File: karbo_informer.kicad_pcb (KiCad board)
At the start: 2 copper layers, 12 parts, among them IC1 MAX7219, IC2 MAX7219, P1 USB_OTG

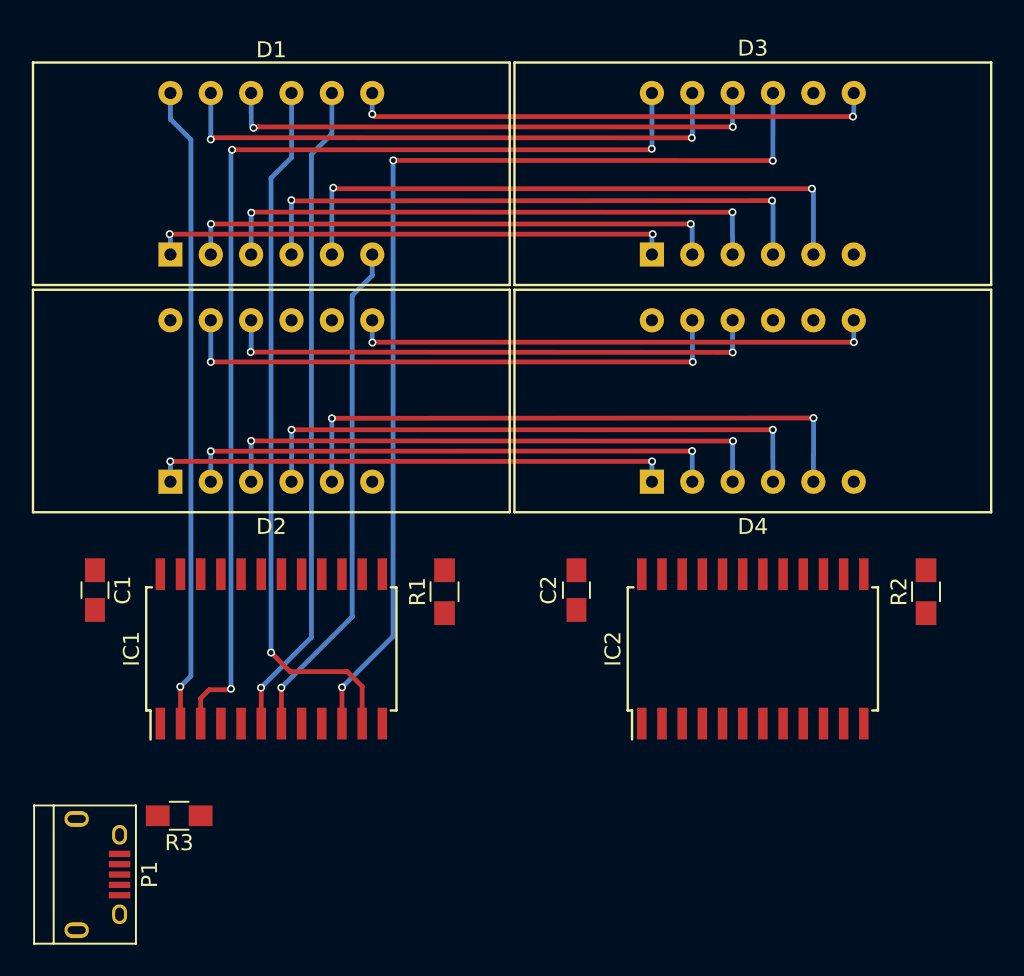
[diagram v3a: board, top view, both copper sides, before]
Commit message: Wire for DIG7 to MAX7219 in the buy line
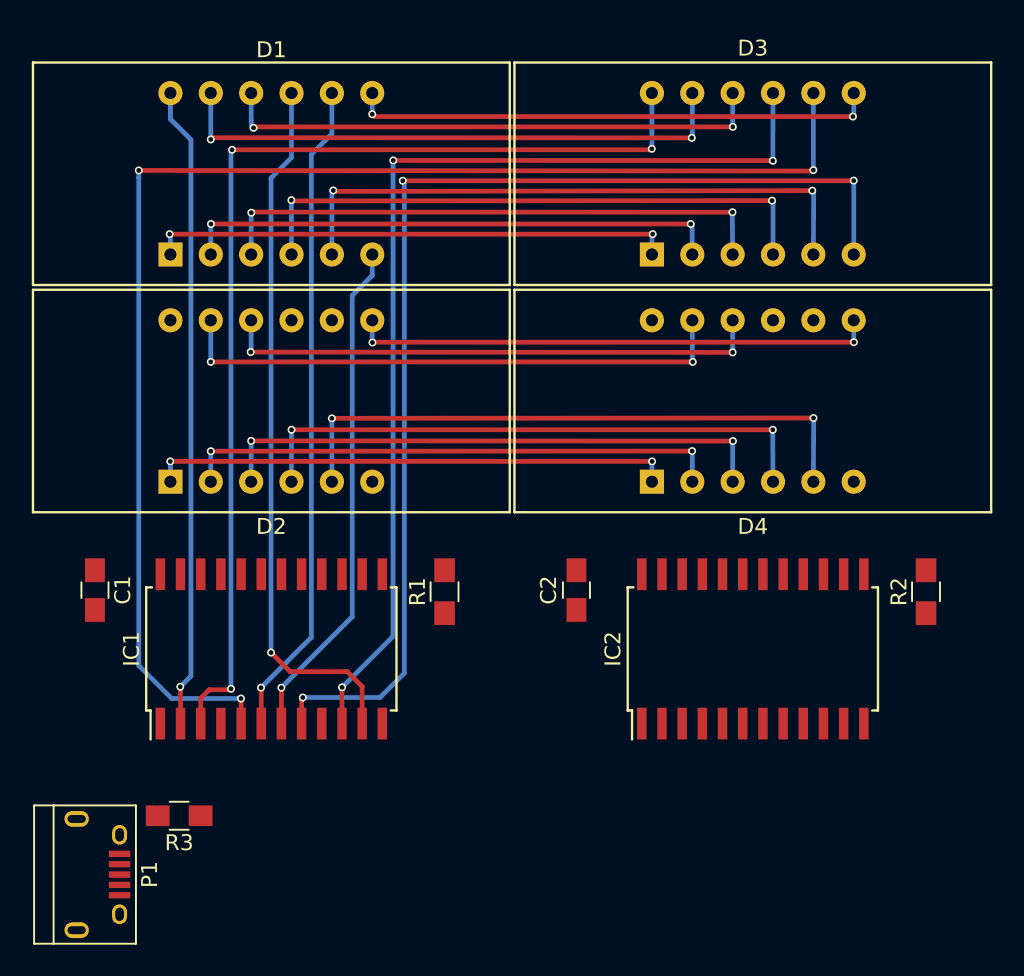
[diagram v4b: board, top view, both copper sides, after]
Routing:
- net /B_DIG_6: track 0.00 -> 87.4 mm, vias 0 -> 3
- net /B_DIG_7: track 0.00 -> 72.8 mm, vias 0 -> 3
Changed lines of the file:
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@@
   (general
     (links 69)
-    (no_connects 47)
+    (no_connects 45)
     (area 0 0 0 0)
     (thickness 1.6)
     (drawings 0)
-    (tracks 157)
+    (tracks 181)
     (zones 0)
     (modules 12)
@@
   (segment (start 42.07 33.98) (end 42.06 30.56) (width 0.3) (layer B.Cu) (net 4))
   (segment (start 42.06 30.56) (end 42.07 30.55) (width 0.3) (layer B.Cu) (net 4))
-  (segment (start 44.61 33.98) (end 44.61 29.87) (width 0.3) (layer B.Cu) (net 5))
-  (segment (start 74.91 29.93) (end 74.91 33.98) (width 0.3) (layer B.Cu) (net 5))
-  (segment (start 74.82 29.84) (end 74.91 29.93) (width 0.3) (layer B.Cu) (net 5))
-  (via (at 74.82 29.84) (size 0.5) (drill 0.3) (layers F.Cu B.Cu) (net 5))
-  (segment (start 44.76 29.84) (end 74.82 29.84) (width 0.3) (layer F.Cu) (net 5))
-  (segment (start 44.7 29.78) (end 44.76 29.84) (width 0.3) (layer F.Cu) (net 5))
-  (via (at 44.7 29.78) (size 0.5) (drill 0.3) (layers F.Cu B.Cu) (net 5))
-  (segment (start 44.61 29.87) (end 44.7 29.78) (width 0.3) (layer B.Cu) (net 5))
+  (segment (start 44.61 33.98) (end 44.61 30.04) (width 0.3) (layer B.Cu) (net 5) (status 400000))
+  (segment (start 74.93 30.05) (end 74.91 33.98) (width 0.3) (layer B.Cu) (net 5) (status 800000))
+  (segment (start 74.84 29.96) (end 74.93 30.05) (width 0.3) (layer B.Cu) (net 5))
+  (via (at 74.84 29.96) (size 0.5) (drill 0.3) (layers F.Cu B.Cu) (net 5))
+  (segment (start 44.76 30.01) (end 74.84 29.96) (width 0.3) (layer F.Cu) (net 5))
+  (segment (start 44.7 29.95) (end 44.76 30.01) (width 0.3) (layer F.Cu) (net 5))
+  (via (at 44.7 29.95) (size 0.5) (drill 0.3) (layers F.Cu B.Cu) (net 5))
+  (segment (start 44.61 30.04) (end 44.7 29.95) (width 0.3) (layer B.Cu) (net 5))
   (segment (start 47.15 33.98) (end 47.15 35.3) (width 0.3) (layer B.Cu) (net 6))
   (segment (start 41.435 61.245) (end 41.435 63.5) (width 0.3) (layer F.Cu) (net 6))
@@
   (segment (start 47.18 39.5) (end 77.46 39.5) (width 0.3) (layer F.Cu) (net 24))
   (via (at 47.16 39.52) (size 0.5) (drill 0.3) (layers F.Cu B.Cu) (net 24))
+  (segment (start 74.91 23.82) (end 74.91 28.67) (width 0.3) (layer B.Cu) (net 25) (status 400000))
+  (segment (start 38.895 61.925) (end 38.895 63.5) (width 0.3) (layer F.Cu) (net 25) (status 800000))
+  (segment (start 38.89 61.92) (end 38.895 61.925) (width 0.3) (layer F.Cu) (net 25))
+  (via (at 38.89 61.92) (size 0.5) (drill 0.3) (layers F.Cu B.Cu) (net 25))
+  (segment (start 34.53 61.92) (end 38.89 61.92) (width 0.3) (layer B.Cu) (net 25))
+  (segment (start 32.46 59.85) (end 34.53 61.92) (width 0.3) (layer B.Cu) (net 25))
+  (segment (start 32.46 29.15) (end 32.46 59.85) (width 0.3) (layer B.Cu) (net 25))
+  (segment (start 32.46 28.69) (end 32.46 29.15) (width 0.3) (layer B.Cu) (net 25))
+  (via (at 32.46 28.69) (size 0.5) (drill 0.3) (layers F.Cu B.Cu) (net 25))
+  (segment (start 74.85 28.73) (end 32.46 28.69) (width 0.3) (layer F.Cu) (net 25))
+  (segment (start 74.91 28.67) (end 74.85 28.73) (width 0.3) (layer F.Cu) (net 25))
+  (via (at 74.91 28.67) (size 0.5) (drill 0.3) (layers F.Cu B.Cu) (net 25))
   (segment (start 36.355 61.905) (end 36.355 63.5) (width 0.3) (layer F.Cu) (net 26))
   (segment (start 36.89 61.37) (end 36.355 61.905) (width 0.3) (layer F.Cu) (net 26))
@@
   (segment (start 48.47 28.06) (end 48.46 28.07) (width 0.3) (layer B.Cu) (net 27))
   (segment (start 72.37 23.82) (end 72.36 28.08) (width 0.3) (layer B.Cu) (net 27) (status 400000))
+  (segment (start 77.45 33.98) (end 77.45 29.33) (width 0.3) (layer B.Cu) (net 33) (status 400000))
+  (segment (start 42.705 61.935) (end 42.705 63.5) (width 0.3) (layer F.Cu) (net 33) (status 800000))
+  (segment (start 42.78 61.86) (end 42.705 61.935) (width 0.3) (layer F.Cu) (net 33))
+  (via (at 42.78 61.86) (size 0.5) (drill 0.3) (layers F.Cu B.Cu) (net 33))
+  (segment (start 47.64 61.86) (end 42.78 61.86) (width 0.3) (layer B.Cu) (net 33))
+  (segment (start 49.17 60.33) (end 47.64 61.86) (width 0.3) (layer B.Cu) (net 33))
+  (segment (start 49.17 29.44) (end 49.17 60.33) (width 0.3) (layer B.Cu) (net 33))
+  (segment (start 49.07 29.34) (end 49.17 29.44) (width 0.3) (layer B.Cu) (net 33))
+  (via (at 49.07 29.34) (size 0.5) (drill 0.3) (layers F.Cu B.Cu) (net 33))
+  (segment (start 77.44 29.34) (end 49.07 29.34) (width 0.3) (layer F.Cu) (net 33))
+  (segment (start 77.45 29.33) (end 77.44 29.34) (width 0.3) (layer F.Cu) (net 33))
+  (via (at 77.45 29.33) (size 0.5) (drill 0.3) (layers F.Cu B.Cu) (net 33))
 )

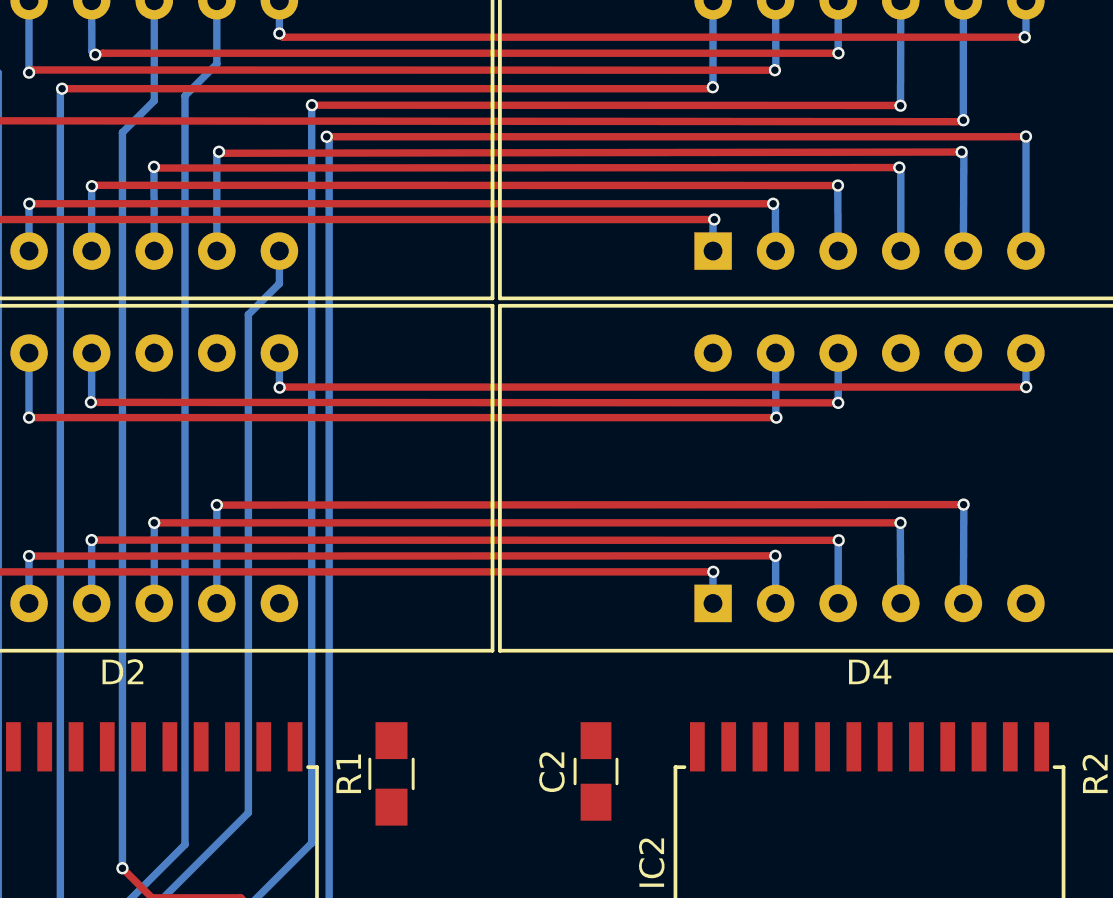
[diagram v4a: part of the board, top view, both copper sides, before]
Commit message: Wire for SEG_G to MAX7219 in the buy line
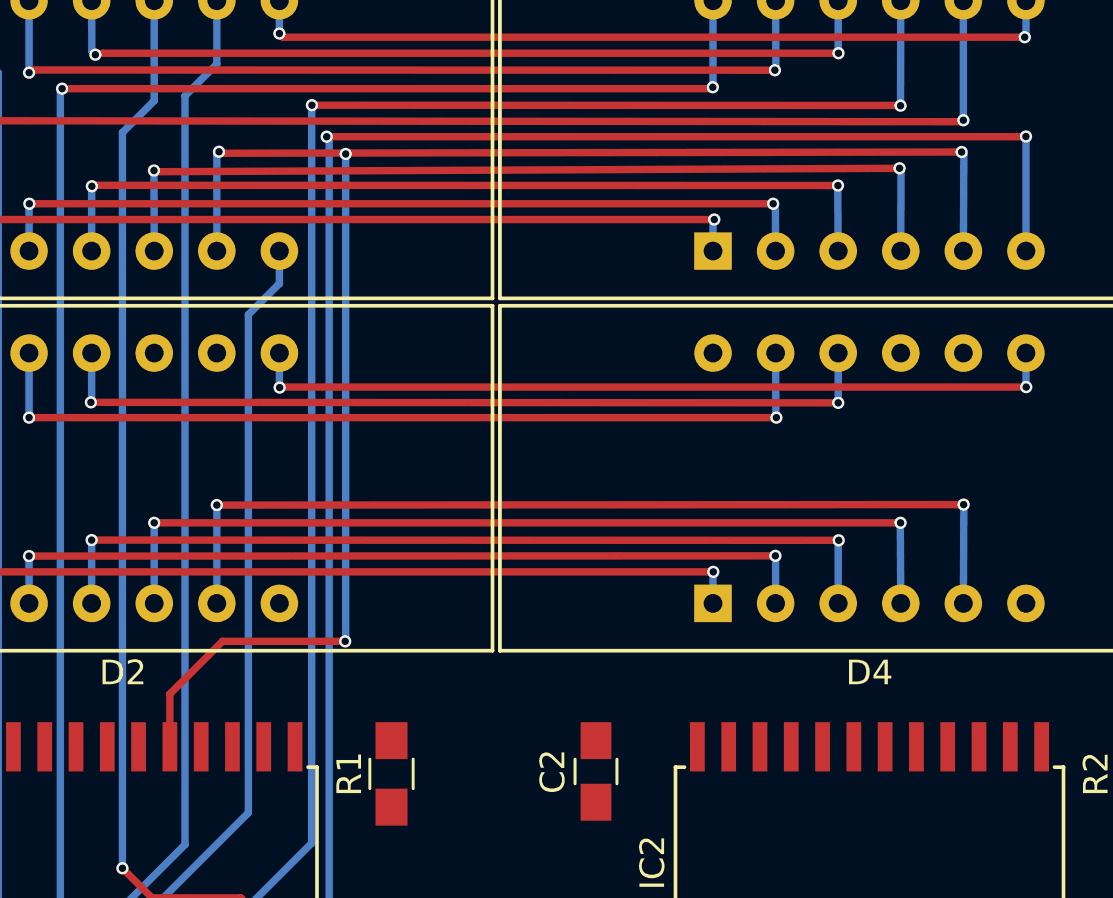
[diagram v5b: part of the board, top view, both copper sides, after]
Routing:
- net /B_SEG_G: track 38.3 -> 68.3 mm, vias 2 -> 4
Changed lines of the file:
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@@
   (general
     (links 69)
-    (no_connects 45)
+    (no_connects 44)
     (area 0 0 0 0)
     (thickness 1.6)
     (drawings 0)
-    (tracks 181)
+    (tracks 191)
     (zones 0)
     (modules 12)
@@
   (segment (start 37 32.06) (end 67.19 32.06) (width 0.3) (layer F.Cu) (net 3))
   (via (at 37 32.06) (size 0.5) (drill 0.3) (layers F.Cu B.Cu) (net 3))
-  (via (at 42.06 30.56) (size 0.5) (drill 0.3) (layers F.Cu B.Cu) (net 4))
-  (segment (start 72.37 33.98) (end 72.37 30.65) (width 0.3) (layer B.Cu) (net 4))
-  (segment (start 72.31 30.59) (end 72.37 30.65) (width 0.3) (layer B.Cu) (net 4))
-  (via (at 72.31 30.59) (size 0.5) (drill 0.3) (layers F.Cu B.Cu) (net 4))
-  (segment (start 42.11 30.61) (end 72.31 30.59) (width 0.3) (layer F.Cu) (net 4))
-  (segment (start 42.11 30.61) (end 42.06 30.56) (width 0.3) (layer F.Cu) (net 4))
-  (segment (start 42.07 33.98) (end 42.06 30.56) (width 0.3) (layer B.Cu) (net 4))
-  (segment (start 42.06 30.56) (end 42.07 30.55) (width 0.3) (layer B.Cu) (net 4))
+  (via (at 42.06 30.71) (size 0.5) (drill 0.3) (layers F.Cu B.Cu) (net 4))
+  (segment (start 72.37 33.98) (end 72.38 30.68) (width 0.3) (layer B.Cu) (net 4) (status 400000))
+  (segment (start 72.32 30.62) (end 72.38 30.68) (width 0.3) (layer B.Cu) (net 4))
+  (via (at 72.32 30.62) (size 0.5) (drill 0.3) (layers F.Cu B.Cu) (net 4))
+  (segment (start 42.11 30.76) (end 72.32 30.62) (width 0.3) (layer F.Cu) (net 4))
+  (segment (start 42.11 30.76) (end 42.06 30.71) (width 0.3) (layer F.Cu) (net 4))
+  (segment (start 42.07 33.98) (end 42.06 30.71) (width 0.3) (layer B.Cu) (net 4) (status 400000))
+  (segment (start 42.06 30.71) (end 42.07 30.7) (width 0.3) (layer B.Cu) (net 4))
+  (via (at 49.84 30.04) (size 0.5) (drill 0.3) (layers F.Cu B.Cu) (net 5))
+  (segment (start 42.705 51.955) (end 44.84 49.82) (width 0.3) (layer F.Cu) (net 5))
+  (segment (start 44.84 49.82) (end 49.82 49.82) (width 0.3) (layer F.Cu) (net 5))
+  (via (at 49.82 49.82) (size 0.5) (drill 0.3) (layers F.Cu B.Cu) (net 5))
+  (segment (start 49.82 49.82) (end 49.84 49.8) (width 0.3) (layer B.Cu) (net 5))
+  (segment (start 49.84 49.8) (end 49.84 30.04) (width 0.3) (layer B.Cu) (net 5))
+  (segment (start 42.705 54.1) (end 42.705 51.955) (width 0.3) (layer F.Cu) (net 5) (status 400000))
+  (segment (start 49.829936 30.029936) (end 49.829936 30.001573) (width 0.3) (layer F.Cu) (net 5))
+  (segment (start 49.84 30.04) (end 49.829936 30.029936) (width 0.3) (layer F.Cu) (net 5))
   (segment (start 44.61 33.98) (end 44.61 30.04) (width 0.3) (layer B.Cu) (net 5) (status 400000))
   (segment (start 74.93 30.05) (end 74.91 33.98) (width 0.3) (layer B.Cu) (net 5) (status 800000))
   (segment (start 74.84 29.96) (end 74.93 30.05) (width 0.3) (layer B.Cu) (net 5))
   (via (at 74.84 29.96) (size 0.5) (drill 0.3) (layers F.Cu B.Cu) (net 5))
-  (segment (start 44.76 30.01) (end 74.84 29.96) (width 0.3) (layer F.Cu) (net 5))
+  (segment (start 44.76 30.01) (end 49.829936 30.001573) (width 0.3) (layer F.Cu) (net 5))
+  (segment (start 49.829936 30.001573) (end 74.84 29.96) (width 0.3) (layer F.Cu) (net 5))
   (segment (start 44.7 29.95) (end 44.76 30.01) (width 0.3) (layer F.Cu) (net 5))
   (via (at 44.7 29.95) (size 0.5) (drill 0.3) (layers F.Cu B.Cu) (net 5))
